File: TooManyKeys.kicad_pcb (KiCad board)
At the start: 2 copper layers, 20.8 x 71.8 mm, 67 parts

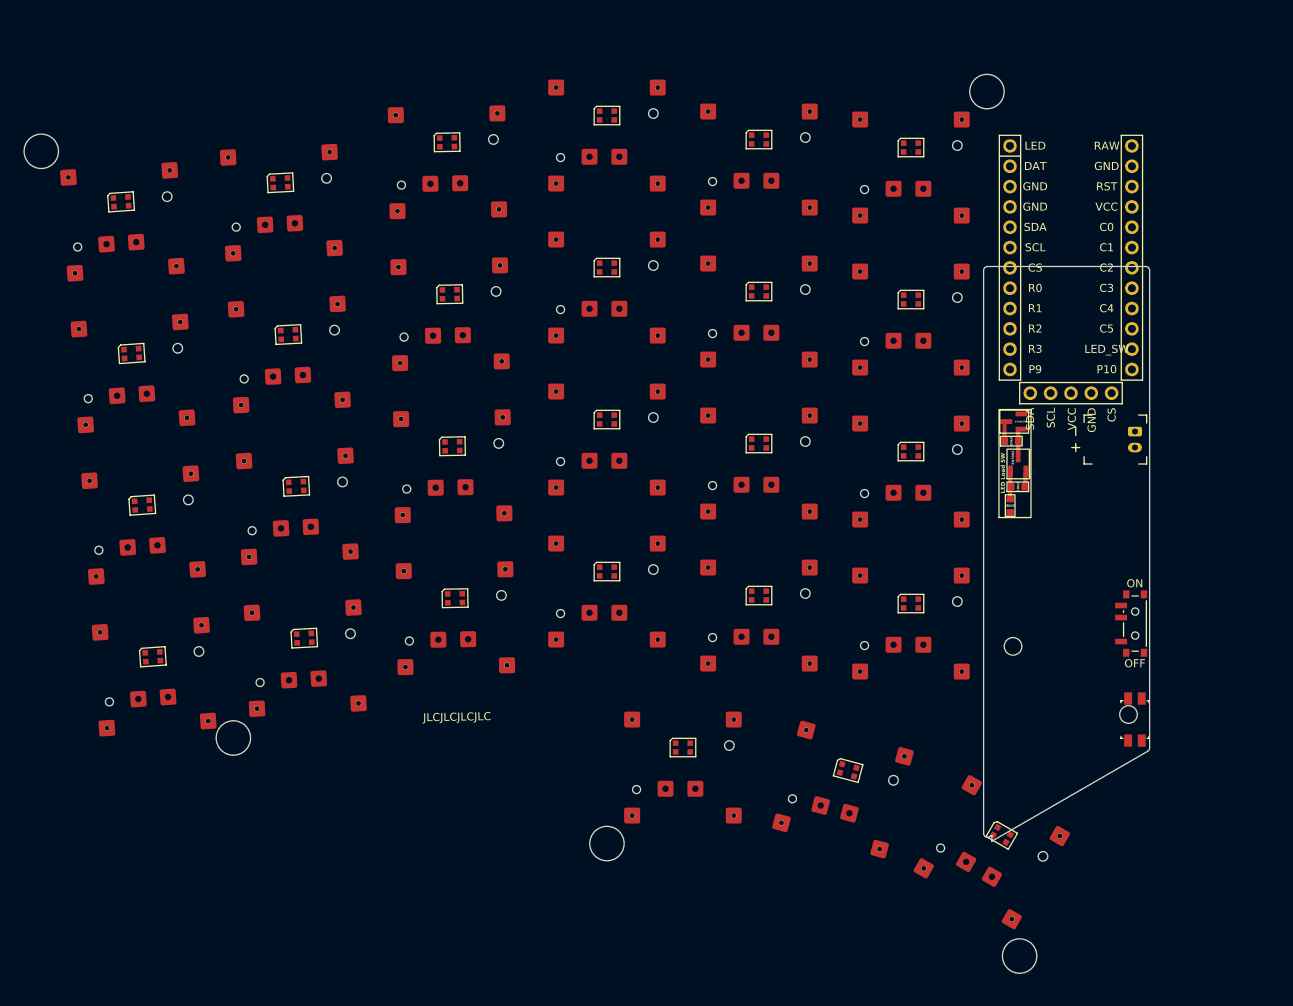
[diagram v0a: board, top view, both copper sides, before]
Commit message: Add BAV70 field and rotary, work on outlines.
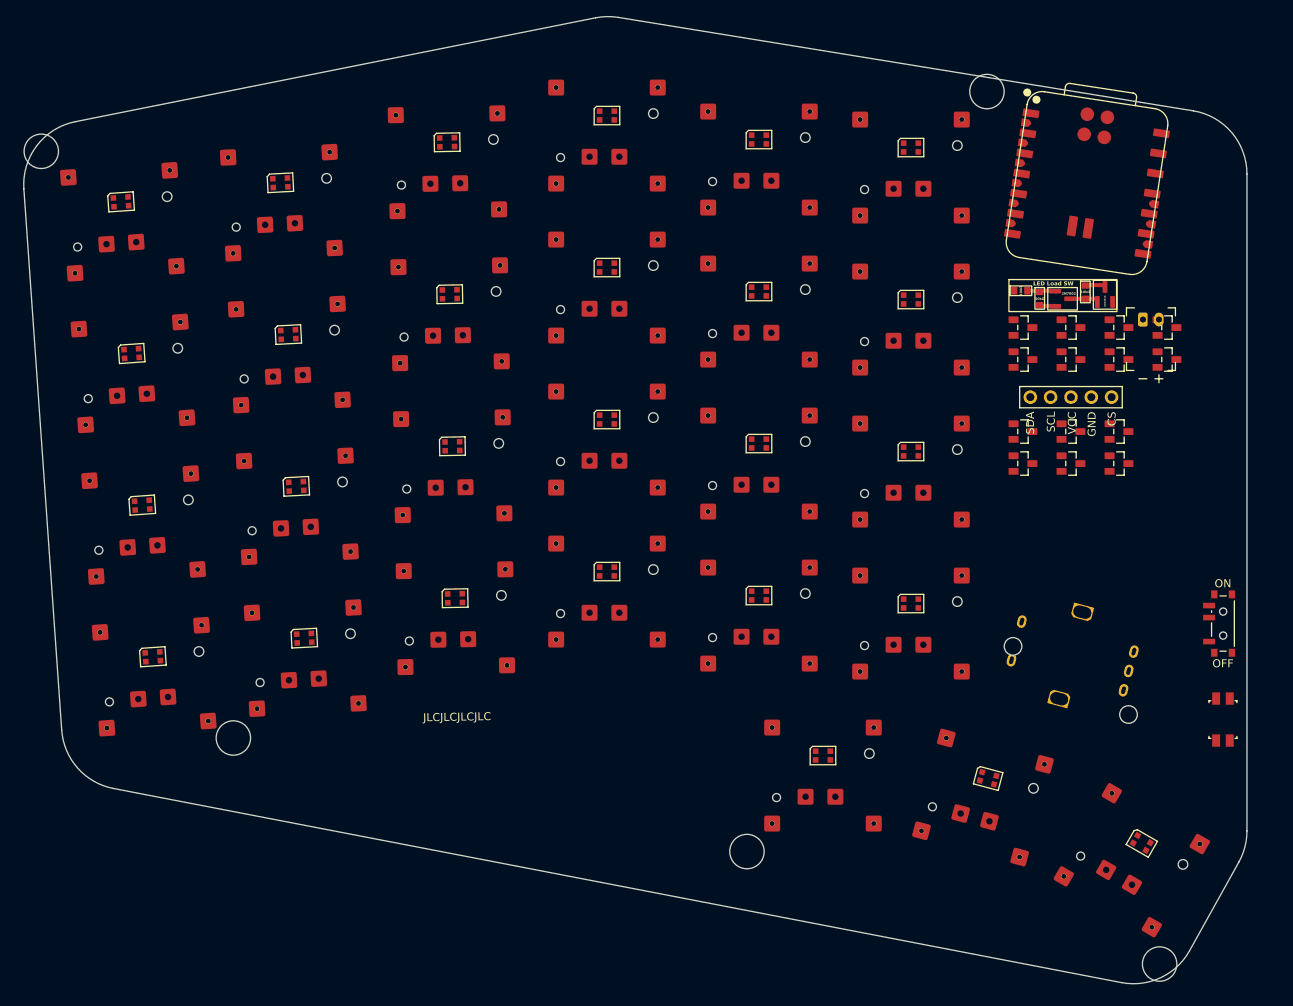
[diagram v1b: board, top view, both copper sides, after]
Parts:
- added D1: BAV70, BAV70 SOT23, F.Cu at (168.6, 116.4)
- added D10: BAV70, BAV70 SOT23, F.Cu at (168.6, 133.4)
- added D11: BAV70, BAV70 SOT23, F.Cu at (174.6, 133.4)
- added D12: BAV70, BAV70 SOT23, F.Cu at (180.6, 133.4)
- added D13: BAV70, BAV70 SOT23, F.Cu at (186.6, 116.4)
- added D14: BAV70, BAV70 SOT23, F.Cu at (186.6, 120.4)
- added D2: BAV70, BAV70 SOT23, F.Cu at (174.6, 116.4)
- added D3: BAV70, BAV70 SOT23, F.Cu at (180.6, 116.4)
- added D4: BAV70, BAV70 SOT23, F.Cu at (168.6, 120.4)
- added D5: BAV70, BAV70 SOT23, F.Cu at (174.6, 120.4)
- added D6: BAV70, BAV70 SOT23, F.Cu at (180.6, 120.4)
- added D7: BAV70, BAV70 SOT23, F.Cu at (168.6, 129.4)
- added D8: BAV70, BAV70 SOT23, F.Cu at (174.6, 129.4)
- added D9: BAV70, BAV70 SOT23, F.Cu at (180.6, 129.4)
- added RE1: , ceoloide:rotary_encoder_ec11_ec12, F.Cu at (174.6, 157.3)
- MCU1: footprint ceoloide:mcu_nice_nano -> XIAO-nRF52840-Plus-SMD
- moved XX1 21.8 mm to (173.6, 112.4), turned to 0 degrees
- moved LED26 17.5 mm to (164.2, 172.7)
- moved MH7 17.5 mm to (185.7, 195.9)
- moved LED27 17.5 mm to (183.5, 180.8)
- moved S27 17.5 mm to (182.2, 182.9)
- moved S26 17.5 mm to (163.6, 175.1)
- moved LED25 17.5 mm to (143.6, 169.9)
- moved MH6 17.5 mm to (134.1, 181.9)
- moved S25 17.5 mm to (143.6, 172.4)
- moved JST1 15.1 mm to (184.6, 115.4), turned to 0 degrees
- moved PWR1 11.0 mm to (193.6, 153.4)
- moved RST1 11.0 mm to (193.6, 165.4)
- moved MCU1 8.25 mm to (176.6, 98.4), turned to 81.3 degrees
- moved DISP1 0.50 mm to (174.6, 108.4)
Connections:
- net DAT renamed P1.07
- net LED renamed DIO
- net P10 renamed 3V3
- net R0 renamed P1.01
- net R1 renamed P0.19
- net R2 renamed P0.15
- net far_fan renamed thumb_far_fan
- net index_bottom renamed finger_index_bottom
- net index_home renamed finger_index_home
- net index_num renamed finger_index_num
- net index_top renamed finger_index_top
- net inner_bottom renamed finger_inner_bottom
- net inner_home renamed finger_inner_home
- net inner_num renamed finger_inner_num
- net inner_top renamed finger_inner_top
- net mid_fan renamed thumb_mid_fan
- net middle_bottom renamed finger_middle_bottom
- net middle_home renamed finger_middle_home
- net middle_num renamed finger_middle_num
- net middle_top renamed finger_middle_top
- net near_fan renamed thumb_near_fan
- net outer_bottom renamed finger_outer_bottom
- net outer_home renamed finger_outer_home
- net outer_num renamed finger_outer_num
- net outer_top renamed finger_outer_top
- net pinky_bottom renamed finger_pinky_bottom
- net pinky_home renamed finger_pinky_home
- net pinky_num renamed finger_pinky_num
- net pinky_top renamed finger_pinky_top
- net ring_bottom renamed finger_ring_bottom
- net ring_home renamed finger_ring_home
- net ring_num renamed finger_ring_num
- net ring_top renamed finger_ring_top
- MCU1 pad 1: RAW -> P0.02
- MCU1 pad 10: C5 -> P1.14
- MCU1 pad 11: LED_SW -> P1.15
- MCU1 pad 13: P9 -> GND
- MCU1 pad 14: R3 -> 5V
- MCU1 pad 18: CS -> P0.09
- MCU1 pad 19: SCL -> P0.10
- MCU1 pad 2: GND -> P0.03
- MCU1 pad 20: SDA -> P0.31
- MCU1 pad 21: GND -> P1.03
- MCU1 pad 22: GND -> P1.05
- MCU1 pad 3: RST -> P0.28
- MCU1 pad 4: VCC -> P0.29
- MCU1 pad 5: C0 -> P0.04
- MCU1 pad 6: C1 -> P0.05
- MCU1 pad 7: C2 -> P1.11
- MCU1 pad 8: C3 -> P1.12
- MCU1 pad 9: C4 -> P1.13
- S25 pad 1: C3 -> C2
- S26 pad 1: C4 -> C3
- S27 pad 1: C5 -> C4
- XX1 pad 2: RAW -> 5V
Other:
- board size 20.8 x 71.8 mm -> 152.9 x 120.9 mm

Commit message: Add CKW12 Roller Encoder Footprint.
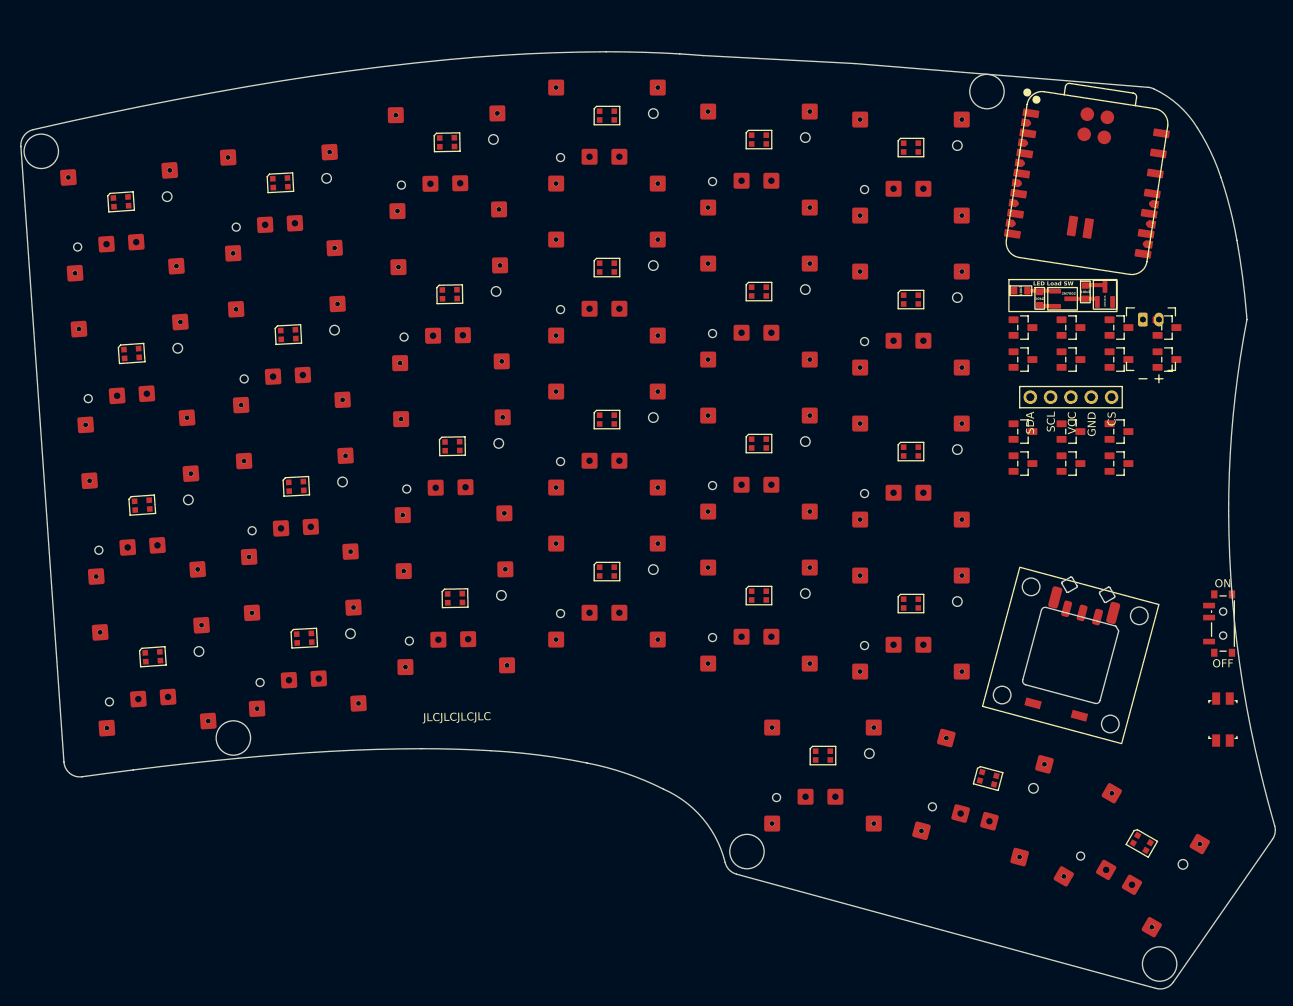
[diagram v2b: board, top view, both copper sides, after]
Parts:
- removed MH6, MH7: , ceoloide:mounting_hole_npth
- RE1: footprint ceoloide:rotary_encoder_ec11_ec12 -> CKW12
- moved MH1 136.3 mm to (45.9, 94.3), turned to 4 degrees
- moved MH3 118.4 mm to (164.1, 86.9), turned to 0 degrees
- moved MH2 111.9 mm to (69.9, 167.7), turned to 3 degrees
- moved MH5 111.2 mm to (185.7, 195.9), turned to -30 degrees
- moved MH4 65.7 mm to (134.1, 181.9), turned to 0 degrees
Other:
- board size 152.9 x 120.9 mm -> 156.8 x 117.1 mm

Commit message: Add nets to MCU, fix diode assignments, work on LEDs.
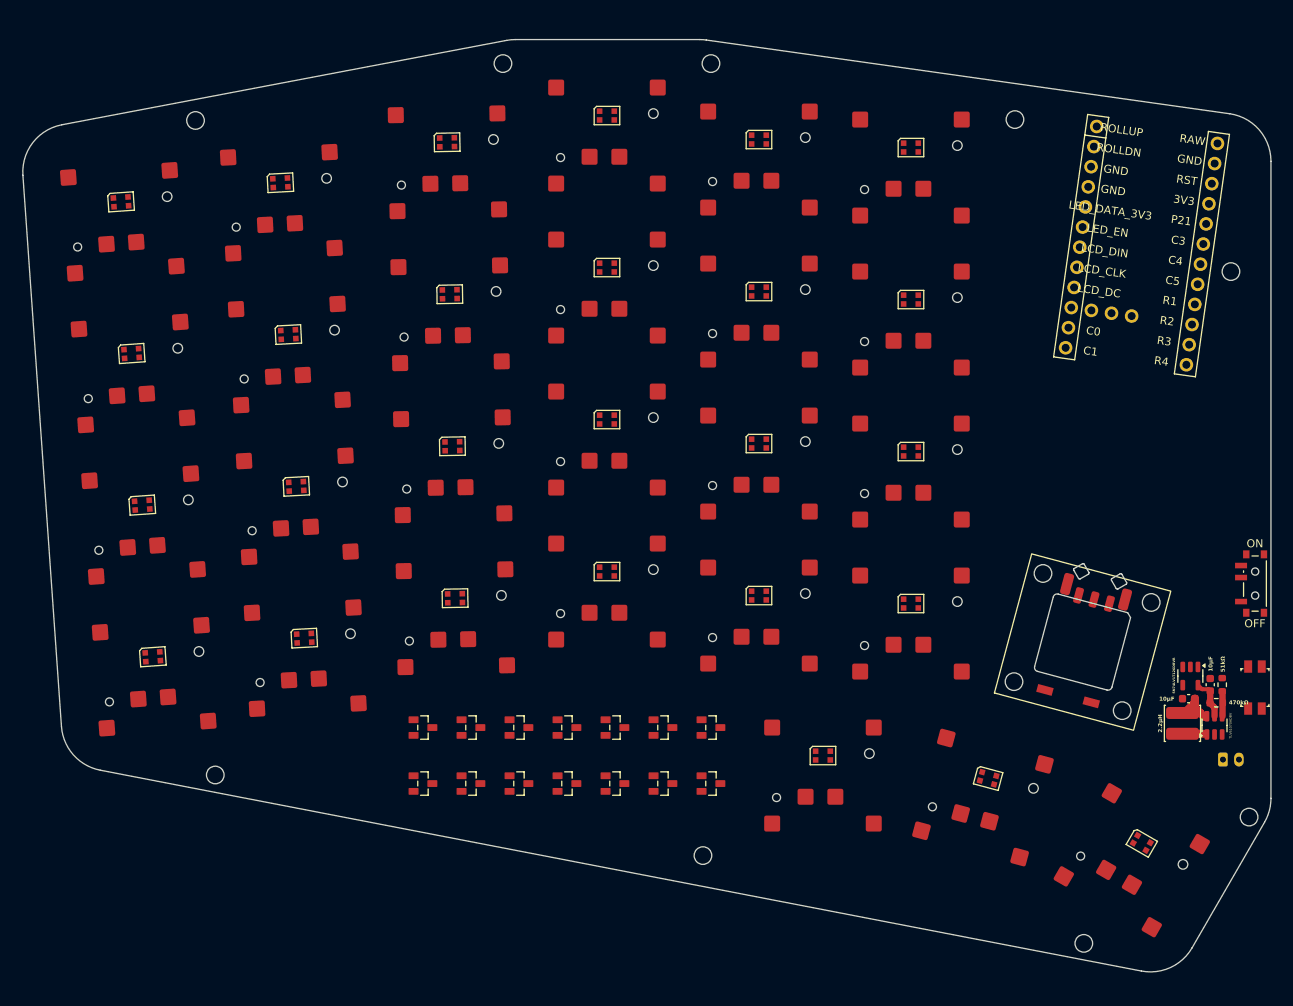
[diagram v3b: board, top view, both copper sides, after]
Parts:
- removed DISP1: , ceoloide:display_nice_view
- removed XX1: , LED_Load_SW
- added C1: 10μF, Capacitor_SMD:C_0603_1608Metric, F.Cu at (189.3, 162.7)
- added C2: 10μF, Capacitor_SMD:C_0603_1608Metric, F.Cu at (192.0, 161.0)
- added L1: 2.2μH, huntercook:L_CJIANG_FTC404030S_4.1x4.1x3.0_SMD, F.Cu at (188.5, 165.8)
- added MH6: , ceoloide:mounting_hole_npth, F.Cu at (194.6, 109.4)
- added MH7: , ceoloide:mounting_hole_npth, F.Cu at (128.6, 182.4)
- added MH8: , ceoloide:mounting_hole_npth, F.Cu at (176.2, 193.3)
- added MH9: , ceoloide:mounting_hole_npth, F.Cu at (196.9, 177.5)
- added R1: 470kΩ, Resistor_SMD:R_0603_1608Metric, F.Cu at (192.8, 163.3)
- added R2: 51kΩ, Resistor_SMD:R_0603_1608Metric, F.Cu at (193.5, 161.0)
- added U1: TLV61070ADBV, Package_TO_SOT_SMD:SOT-23-6, F.Cu at (192.5, 166.1)
- added U2: SN74LV1T126DBVR, Package_TO_SOT_SMD:SOT-23-5, F.Cu at (189.5, 159.9)
- JST1: moved to B.Cu
- MCU1: footprint XIAO-nRF52840-Plus-SMD -> ceoloide:mcu_nice_nano
- moved MH5 107.1 mm to (167.6, 90.4), turned to 0 degrees
- moved MH4 98.6 mm to (129.6, 83.4)
- moved D8 92.2 mm to (93.6, 173.4)
- moved D9 92.2 mm to (99.6, 173.4)
- moved D1 90.1 mm to (93.6, 166.4)
- moved D2 90.1 mm to (99.6, 166.4)
- moved D3 90.1 mm to (105.6, 166.4)
- moved D13 85.0 mm to (123.6, 173.4)
- moved D14 77.8 mm to (129.6, 173.4)
- moved D10 74.6 mm to (105.6, 173.4)
- moved D11 74.6 mm to (111.6, 173.4)
- moved D12 74.6 mm to (117.6, 173.4)
- moved D4 73.2 mm to (111.6, 166.4)
- moved D5 73.2 mm to (117.6, 166.4)
- moved D6 73.2 mm to (123.6, 166.4)
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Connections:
- net CLK renamed LCD_CS
- net P0.04 renamed P21
- net P0.09 renamed LCD_DIN
- net P0.10 renamed LED_EN
- net P0.15 renamed LCD_BL
- net P0.19 renamed LCD_DC
- net P1.01 renamed LCD_CLK
- net P1.14 renamed R2
- net P1.15 renamed R3
- LED27 pad 1: LED_START -> LED_DATA_5V
- MCU1 pad 1: P0.02 -> RAW
- MCU1 pad 12: 3V3 -> R4
- MCU1 pad 13: GND -> C1
- MCU1 pad 14: 5V -> C0
- MCU1 pad 2: P0.03 -> GND
- MCU1 pad 20: P0.31 -> LED_DATA_3V3
- MCU1 pad 21: P1.03 -> GND
- MCU1 pad 22: P1.05 -> GND
- MCU1 pad 23: P1.07 -> ROLLDN
- MCU1 pad 24: DIO -> ROLLUP
- MCU1 pad 26: RST -> LCD_RST
- MCU1 pad 27: GND -> C2
- MCU1 pad 3: P0.28 -> RST
- MCU1 pad 4: P0.29 -> 3V3
- MCU1 pad 6: P0.05 -> C3
- MCU1 pad 7: P1.11 -> C4
- MCU1 pad 8: P1.12 -> C5
- MCU1 pad 9: P1.13 -> R1
- RE1 pad A: ENC_UP -> ROLLUP
- RE1 pad C: ENC_DN -> ROLLDN
- S1 pad : finger_outer_bottom -> (no net)
- S1 pad 3: (no net) -> GND
- S10 pad : finger_ring_home -> (no net)
- S10 pad 3: (no net) -> GND
- S11 pad : finger_ring_top -> (no net)
- S11 pad 3: (no net) -> GND
- S12 pad : finger_ring_num -> (no net)
- S12 pad 3: (no net) -> GND
- S13 pad : finger_middle_bottom -> (no net)
- S13 pad 3: (no net) -> GND
- S14 pad : finger_middle_home -> (no net)
- S14 pad 3: (no net) -> GND
- S15 pad : finger_middle_top -> (no net)
- S15 pad 3: (no net) -> GND
- S16 pad : finger_middle_num -> (no net)
- S16 pad 3: (no net) -> GND
- S17 pad : finger_index_bottom -> (no net)
- S17 pad 3: (no net) -> GND
- S18 pad : finger_index_home -> (no net)
- S18 pad 3: (no net) -> GND
- S19 pad : finger_index_top -> (no net)
- S19 pad 3: (no net) -> GND
- S2 pad : finger_outer_home -> (no net)
- S2 pad 3: (no net) -> GND
- S20 pad : finger_index_num -> (no net)
- S20 pad 3: (no net) -> GND
- S21 pad : finger_inner_bottom -> (no net)
- S21 pad 3: (no net) -> GND
- S22 pad : finger_inner_home -> (no net)
- S22 pad 3: (no net) -> GND
- S23 pad : finger_inner_top -> (no net)
- S23 pad 3: (no net) -> GND
- S24 pad : finger_inner_num -> (no net)
- S24 pad 3: (no net) -> GND
- S25 pad : thumb_near_fan -> (no net)
- S25 pad 3: (no net) -> GND
- S26 pad : thumb_mid_fan -> (no net)
- S26 pad 3: (no net) -> GND
- S27 pad : thumb_far_fan -> (no net)
- S27 pad 3: (no net) -> GND
- S3 pad : finger_outer_top -> (no net)
- S3 pad 3: (no net) -> GND
- S4 pad : finger_outer_num -> (no net)
- S4 pad 3: (no net) -> GND
- S5 pad : finger_pinky_bottom -> (no net)
- S5 pad 3: (no net) -> GND
- S6 pad : finger_pinky_home -> (no net)
- S6 pad 3: (no net) -> GND
- S7 pad : finger_pinky_top -> (no net)
- S7 pad 3: (no net) -> GND
- S8 pad : finger_pinky_num -> (no net)
- S8 pad 3: (no net) -> GND
- S9 pad : finger_ring_bottom -> (no net)
- S9 pad 3: (no net) -> GND
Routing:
- net RAW: track 0.00 -> 7.58 mm
- net V_OUT: track 0.00 -> 5.28 mm
- net Net-(U1-V_{FB}): track 0.00 -> 3.14 mm
- net Net-(U1-SW): track 0.00 -> 2.75 mm
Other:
- board size 156.8 x 117.1 mm -> 156 x 116.5 mm
- board text removed: "JLCJLCJLCJLC"
